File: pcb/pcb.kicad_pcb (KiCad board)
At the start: 2 copper layers, 61.7 x 71.3 mm, 16 parts, among them J1 Raspberry_Pi_2_3, SW1 SW_GPIO26, SW2 SW_GPIO19, SW3 SW_GPIO22, SW4 SW_GPIO27, SW5 SW_GPIO17

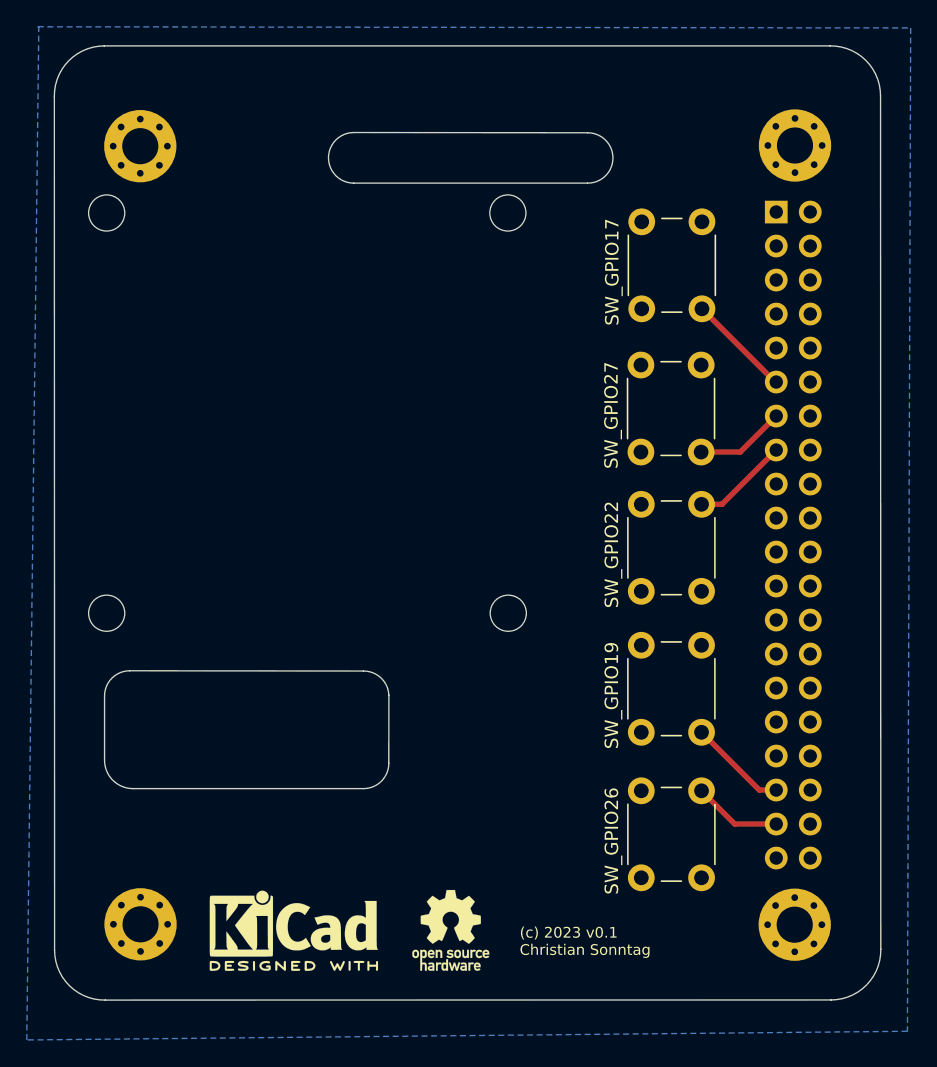
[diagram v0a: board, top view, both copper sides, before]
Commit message: add additional pinheader as alternative to button switches
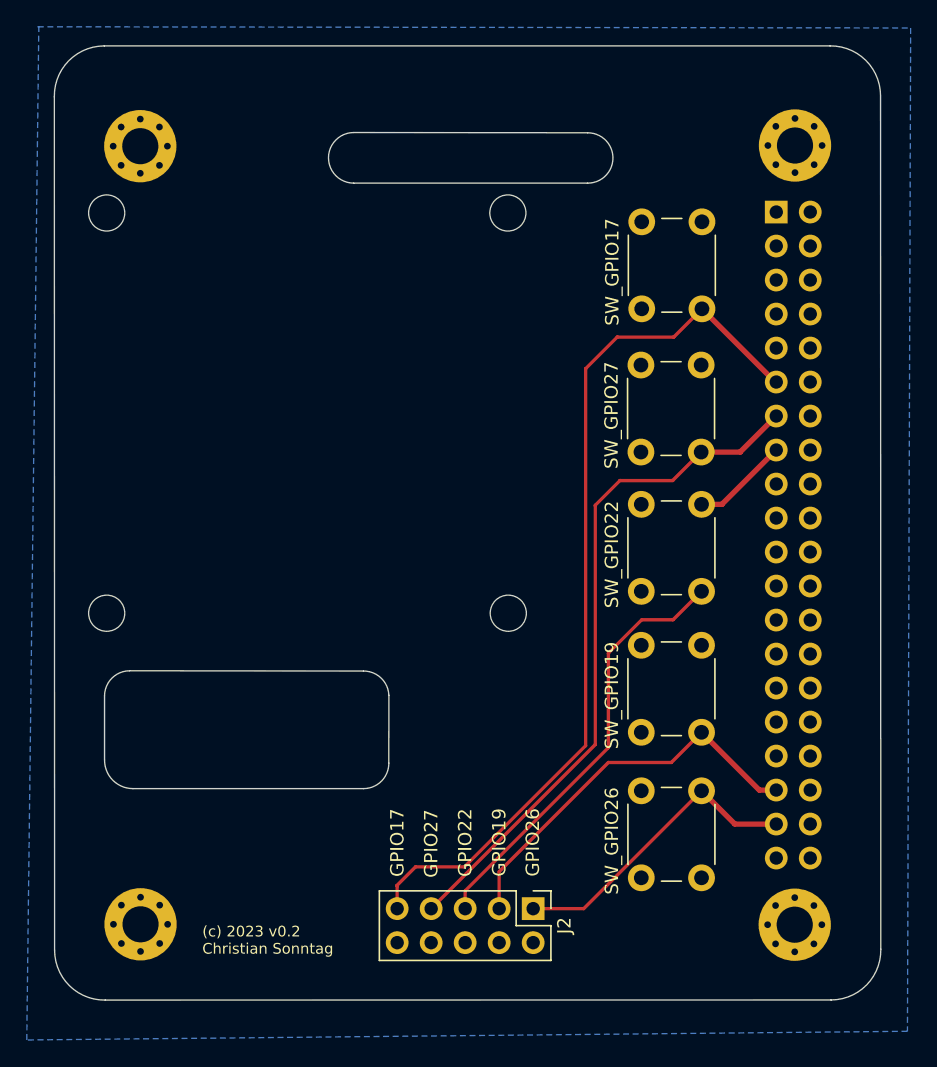
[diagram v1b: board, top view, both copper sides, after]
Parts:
- removed REF**: KiCad-Logo2_5mm_SilkScreen, Symbol:KiCad-Logo2_5mm_SilkScreen
- removed REF**: OSHW-Logo_5.7x6mm_SilkScreen, Symbol:OSHW-Logo_5.7x6mm_SilkScreen
- added J2: Conn_02x05_Odd_Even, Connector_PinHeader_2.54mm:PinHeader_2x05_P2.54mm_Vertical, F.Cu at (88.8, 96.5)
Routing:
- net GPIO17: track 7.82 -> 66.7 mm
- net GPIO27: track 6.72 -> 51.5 mm
- net GPIO22: track 7.26 -> 39.7 mm
- net GPIO19: track 7.37 -> 29.6 mm
- net GPIO26: track 6.61 -> 22.8 mm
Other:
- board text added: "(c) 2023 v0.2 Christian Sonntag"
- board text added: "GPIO17"
- board text added: "GPIO19"
- board text added: "GPIO22"
- board text added: "GPIO26"
- board text added: "GPIO27"
- board text removed: "(c) 2023 v0.1 Christian Sonntag"
